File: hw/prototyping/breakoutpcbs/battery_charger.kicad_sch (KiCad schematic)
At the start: 22 parts, among them J10 Conn_01x03_MountingPin, J14 Conn_01x02, J19 Conn_01x02, J6 Conn_01x05, J9 Screw_Terminal_01x02, Q8 BC337, Q9 BC847, U8 MAX40200AUK, U9 MAX40200AUK

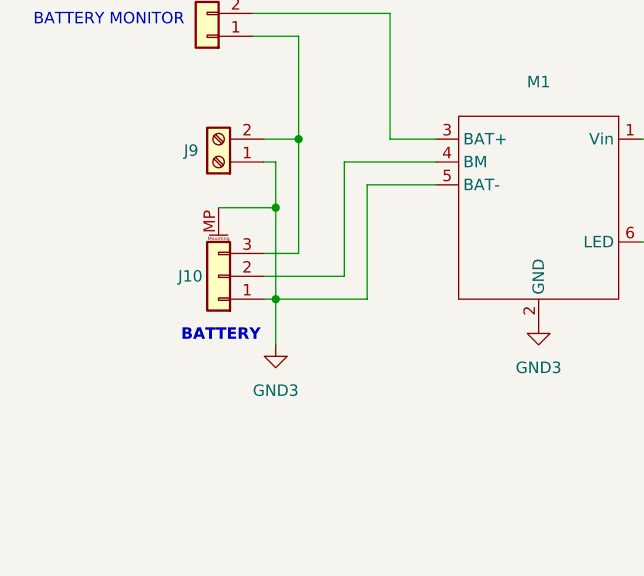
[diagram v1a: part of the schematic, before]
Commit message: reversed balancing connector pin order
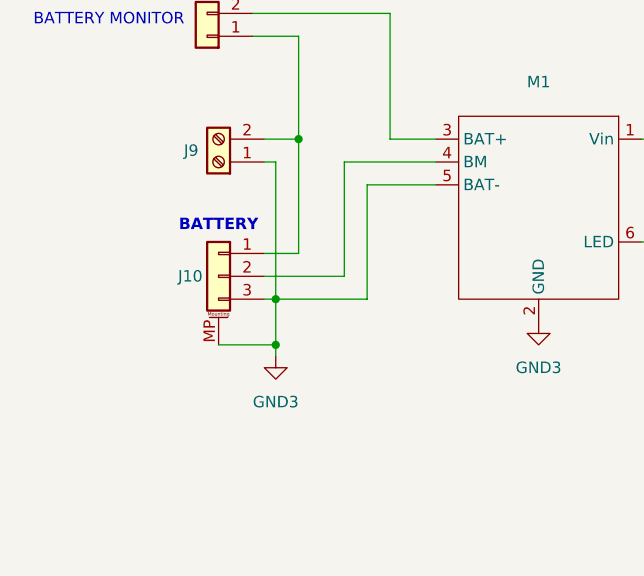
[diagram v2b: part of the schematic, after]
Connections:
- net GND3: now also J10.3 (Pin_3); no longer J10.1 (Pin_1)
- net at J14.1 (Pin_1), J9.2 (Pin_2): now also J10.1 (Pin_1); no longer J10.3 (Pin_3)
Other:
- moved on the sheet: J10
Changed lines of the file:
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@@
 	(text "BATTERY"
 		(exclude_from_sim no)
-		(at 42.164 61.214 0)
+		(at 41.91 49.022 0)
 		(effects
 			(font
@@
 	)
 	(junction
+		(at 48.26 62.23)
+		(diameter 0)
+		(color 0 0 0 0)
+	)
+	(junction
+		(at 128.27 87.63)
+		(diameter 0)
+		(color 0 0 0 0)
+	)
+	(junction
+		(at 186.69 116.84)
+		(diameter 0)
+		(color 0 0 0 0)
+	)
+	(junction
 		(at 48.26 57.15)
 		(diameter 0)
@@
 	)
 	(junction
-		(at 128.27 87.63)
-		(diameter 0)
-		(color 0 0 0 0)
-	)
-	(junction
-		(at 48.26 46.99)
-		(diameter 0)
-		(color 0 0 0 0)
-	)
-	(junction
-		(at 186.69 116.84)
-		(diameter 0)
-		(color 0 0 0 0)
-	)
-	(junction
 		(at 147.32 74.93)
 		(diameter 0)
@@
 	(wire
 		(pts
+			(xy 41.91 62.23) (xy 48.26 62.23)
+		)
+		(stroke
+			(width 0)
+			(type default)
+		)
+	)
+	(wire
+		(pts
 			(xy 60.96 25.4) (xy 60.96 39.37)
 		)
@@
 	(wire
 		(pts
+			(xy 48.26 57.15) (xy 48.26 62.23)
+		)
+		(stroke
+			(width 0)
+			(type default)
+		)
+	)
+	(wire
+		(pts
 			(xy 179.07 53.34) (xy 179.07 50.8)
 		)
@@
 	(wire
 		(pts
-			(xy 41.91 46.99) (xy 48.26 46.99)
-		)
-		(stroke
-			(width 0)
-			(type default)
-		)
-	)
-	(wire
-		(pts
 			(xy 46.99 52.07) (xy 50.8 52.07)
 		)
@@
 	(wire
 		(pts
+			(xy 48.26 57.15) (xy 58.42 57.15)
+		)
+		(stroke
+			(width 0)
+			(type default)
+		)
+	)
+	(wire
+		(pts
 			(xy 45.72 25.4) (xy 60.96 25.4)
 		)
@@
 	(wire
 		(pts
-			(xy 48.26 46.99) (xy 48.26 57.15)
-		)
-		(stroke
-			(width 0)
-			(type default)
-		)
-	)
-	(wire
-		(pts
 			(xy 92.71 87.63) (xy 128.27 87.63)
 		)
@@
 	(wire
 		(pts
-			(xy 48.26 41.91) (xy 48.26 46.99)
-		)
-		(stroke
-			(width 0)
-			(type default)
-		)
-	)
-	(wire
-		(pts
 			(xy 58.42 44.45) (xy 66.04 44.45)
 		)
@@
 	(wire
 		(pts
-			(xy 48.26 57.15) (xy 48.26 62.23)
+			(xy 48.26 41.91) (xy 48.26 57.15)
 		)
 		(stroke
@@
 	(wire
 		(pts
-			(xy 48.26 57.15) (xy 46.99 57.15)
-		)
-		(stroke
-			(width 0)
-			(type default)
-		)
-	)
-	(wire
-		(pts
 			(xy 128.27 87.63) (xy 132.08 87.63)
 		)
@@
 	(wire
 		(pts
-			(xy 48.26 57.15) (xy 58.42 57.15)
+			(xy 46.99 57.15) (xy 48.26 57.15)
 		)
 		(stroke
@@
 		(pts
 			(xy 143.51 77.47) (xy 143.51 74.93)
+		)
+		(stroke
+			(width 0)
+			(type default)
+		)
+	)
+	(wire
+		(pts
+			(xy 48.26 63.5) (xy 48.26 62.23)
 		)
 		(stroke
@@
 	(symbol
 		(lib_id "Connector_Generic_MountingPin:Conn_01x03_MountingPin")
-		(at 41.91 54.61 180)
+		(at 41.91 54.61 0)
+		(mirror y)
 		(unit 1)
 		(exclude_from_sim no)
@@
 		)
 		(property "Value" "Conn_01x03_MountingPin"
-			(at 40.64 55.5243 0)
+			(at 40.64 53.6957 0)
 			(effects
 				(font
@@
 	(symbol
 		(lib_id "power:GND")
-		(at 48.26 62.23 0)
+		(at 48.26 63.5 0)
 		(unit 1)
 		(exclude_from_sim no)
@@
 		(fields_autoplaced yes)
 		(property "Reference" "#PWR047"
+			(at 48.26 69.85 0)
+			(effects
+				(font
+					(size 1.27 1.27)
+				)
+				(hide yes)
+			)
+		)
+		(property "Value" "GND3"
 			(at 48.26 68.58 0)
 			(effects
@@
 					(size 1.27 1.27)
 				)
-				(hide yes)
-			)
-		)
-		(property "Value" "GND3"
-			(at 48.26 67.31 0)
-			(effects
-				(font
-					(size 1.27 1.27)
-				)
 			)
 		)
 		(property "Footprint" ""
-			(at 48.26 62.23 0)
+			(at 48.26 63.5 0)
 			(effects
 				(font
@@
 		)
 		(property "Datasheet" ""
-			(at 48.26 62.23 0)
+			(at 48.26 63.5 0)
 			(effects
 				(font
@@
 		)
 		(property "Description" "Power symbol creates a global label with name \"GND\" , ground"
-			(at 48.26 62.23 0)
-			(effects
-				(font
+			(at 48.26 63.5 0)
+			(effects
+				(font
